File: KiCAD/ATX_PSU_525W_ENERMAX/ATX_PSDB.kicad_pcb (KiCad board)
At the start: 2 copper layers, 160 x 170 mm, 92 parts, among them J1 Fan1, J10 ATX12V1 8 Pin, J11 Current Sens, J12 Molex: 0039281243, J13 12V2, J14 Molex: 0039281243, J15 Potti, J16 Potti, J17 LED Yellow, J18 LED Yellow, J19 Volt Sens, J2 Power On Switch, J20 12V Out, J21 Volt Sens, J22 12V Out, J23 Molex: 0039281243, J24 Current Sens, J25 Current Sens, J26 Molex: 0039281243, J27 Molex: 0039281243, J28 Fan1, J29 Fan1, J3 Standby LED, J30 Potti, J31 Potti, J32 LED Red, J33 LED Orange, J34 Volt Sens, J35 5V Out, J36 Volt Sens, J37 3.3V Out, J38 Screw_Terminal_01x06, J39 Screw_Terminal_01x06, J4 ATX12V1, J40 Current Sens, J41 Current Sens, J42 Screw_Terminal_01x06, J43 Screw_Terminal_01x06, J44 Screw_Terminal_01x12, J5 Potti, J6 LED Yellow, J7 Volt Sens, J8 12V Out, J9 Main ATX 24Pin, Q1 Q_NMOS_DGS, Q2 Q_NMOS_DGS, Q3 Q_NMOS_DGS, Q4 Q_NMOS_DGS, Q5 Q_NMOS_DGS, U1 ACS712xLCTR-20A, U2 ACS712xLCTR-20A, U3 ACS712xLCTR-20A, U4 ACS712xLCTR-20A, U5 ACS712xLCTR-20A

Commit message: cleanup
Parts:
- removed HS1: Heatsink, Heatsink:Heatsink_Stonecold_HS-132_32x14mm_2xFixation1.5mm
- DZ1, DZ2, DZ3, DZ4, DZ5: value D_Zener_ALT -> TSV Protection Diode
- J10: value ATX12V1 8 Pin -> ATX12V1
- J12, J14: value Molex: 0039281243 -> Molex: 12V2
- J23, J26, J27: value Molex: 0039281243 -> Molex: 12V3
- J38: value Screw_Terminal_01x06 -> Terminal: 12V2; footprint TerminalBlock_WAGO:TerminalBlock_WAGO_236-108_1x08_P5.00mm_45Degree -> TerminalBlock_WAGO:TerminalBlock_WAGO_236-106_1x06_P5.00mm_45Degree
- J39: value Screw_Terminal_01x06 -> Terminal: 12V3; footprint TerminalBlock_WAGO:TerminalBlock_WAGO_236-108_1x08_P5.00mm_45Degree -> TerminalBlock_WAGO:TerminalBlock_WAGO_236-106_1x06_P5.00mm_45Degree
- J42: value Screw_Terminal_01x06 -> 5V Terminal; footprint TerminalBlock_WAGO:TerminalBlock_WAGO_236-108_1x08_P5.00mm_45Degree -> TerminalBlock_WAGO:TerminalBlock_WAGO_236-106_1x06_P5.00mm_45Degree
- J43: value Screw_Terminal_01x06 -> 3.3V Terminal; footprint TerminalBlock_WAGO:TerminalBlock_WAGO_236-108_1x08_P5.00mm_45Degree -> TerminalBlock_WAGO:TerminalBlock_WAGO_236-106_1x06_P5.00mm_45Degree
- J44: value Screw_Terminal_01x12 -> Ground Terminal
- Q1, Q2, Q3, Q4, Q5: value Q_NMOS_DGS -> Power N-Mosfet
- REF** (x4): value MountingHole_4.3mm_M4_Pad_Via -> Mounting Hole
- U1, U2, U3, U4, U5: value ACS712xLCTR-20A -> ACS712-20A
- moved REF** 185.8 mm to (83.8, 199.1), turned to 90 degrees
- moved REF** 10.7 mm to (86.4, 214.0)
- moved J13 10.2 mm to (125.7, 152.9)
- moved J26 10.2 mm to (125.7, 185.9)
- moved J12 10.2 mm to (110.5, 152.9)
- moved J14 10.2 mm to (95.2, 152.9)
- moved J23 10.2 mm to (110.5, 185.9)
- moved J27 10.2 mm to (95.2, 185.9)
- moved J38 10.2 mm to (96.0, 169.7)
- moved J39 10.2 mm to (96.5, 203.7)
- moved REF** 8.82 mm to (84.3, 57.7)
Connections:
- REF** pad 1: (no net) -> GND (x4)
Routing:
- net +5V: track 345.8 -> 598.8 mm, vias 0 -> 5
- net +3.3V: track 57.5 -> 45.7 mm
- net Net-(J7-Pad1): vias 0 -> 3
- net Net-(J36-Pad1): vias 0 -> 3
- net Net-(J34-Pad1): vias 0 -> 3
- net Net-(J21-Pad1): vias 0 -> 3
- net Net-(J19-Pad1): vias 0 -> 3
- net Net-(DZ5-Pad1): vias 0 -> 3
- net Net-(DZ4-Pad1): vias 0 -> 3
- net Net-(DZ3-Pad1): vias 0 -> 3
- net Net-(DZ2-Pad1): vias 0 -> 3
- net Net-(DZ1-Pad1): vias 0 -> 3
- net GND: vias 0 -> 67
- net (no net): vias 0 -> 2
- added copper zone on B.Cu, net +12V1
- added copper zone on B.Cu, net +12V2
- added copper zone on B.Cu, net +12V3
- added copper zone on B.Cu, net +3.3V
- added copper zone on B.Cu, net +5V
- added copper zone on B.Cu, net 12V1-
- added copper zone on B.Cu, net 12V2-
- added copper zone on B.Cu, net 12V3-
- added copper zone on B.Cu, net 3.3V-
- added copper zone on B.Cu, net 5V-
- added copper zone on B.Cu, net Net-(DZ1-Pad1)
- added copper zone on B.Cu, net Net-(DZ2-Pad1)
- added copper zone on B.Cu, net Net-(DZ3-Pad1)
- added copper zone on B.Cu, net Net-(DZ4-Pad1)
- added copper zone on B.Cu, net Net-(DZ5-Pad1)
- added copper zone on B.Cu, net Net-(J19-Pad1)
- added copper zone on B.Cu, net Net-(J21-Pad1)
- added copper zone on B.Cu, net Net-(J34-Pad1)
- added copper zone on B.Cu, net Net-(J36-Pad1)
- added copper zone on B.Cu, net Net-(J7-Pad1)

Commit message: labeling
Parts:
- removed the REF** at (224.0, 213.9)
- removed the REF** at (86.4, 214.0)
- added REF**: Mounting Hole, MountingHole:MountingHole_4.3mm_M4_Pad_Via, F.Cu at (223.9, 213.9)
- added REF**: Mounting Hole, MountingHole:MountingHole_4.3mm_M4_Pad_Via, F.Cu at (76.6, 214.0)
- J1: value Fan1 -> Fan 12V
- J2: value Power On Switch -> Power On/Off Switch
- J20: value 12V Out -> 12V2 Out
- J22: value 12V Out -> 12V3 Out
- J28: value Fan1 -> Fan 5V
- J29: value Fan1 -> Fan 3.3V
- J8: value 12V Out -> 12V1 Out
- moved REF** 131.1 mm to (80.4, 68.1)
- moved REF** 8.08 mm to (76.6, 55.4)
- moved REF** 2.07 mm to (223.9, 55.4)
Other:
- board text added: "12V1 Power Rail Input"
- board text added: "12V2 Power Rail Input"
- board text added: "3.3V Input Terminal"
- board text added: "5V Input Terminal"
- board text added: "Fuse Ratings should not exceed 10A each"
- board text added: "Molex"
- board text added: "Power Shunt"
- board text added: "Terminal"
- board text added: "Use Pottis for current limiting"

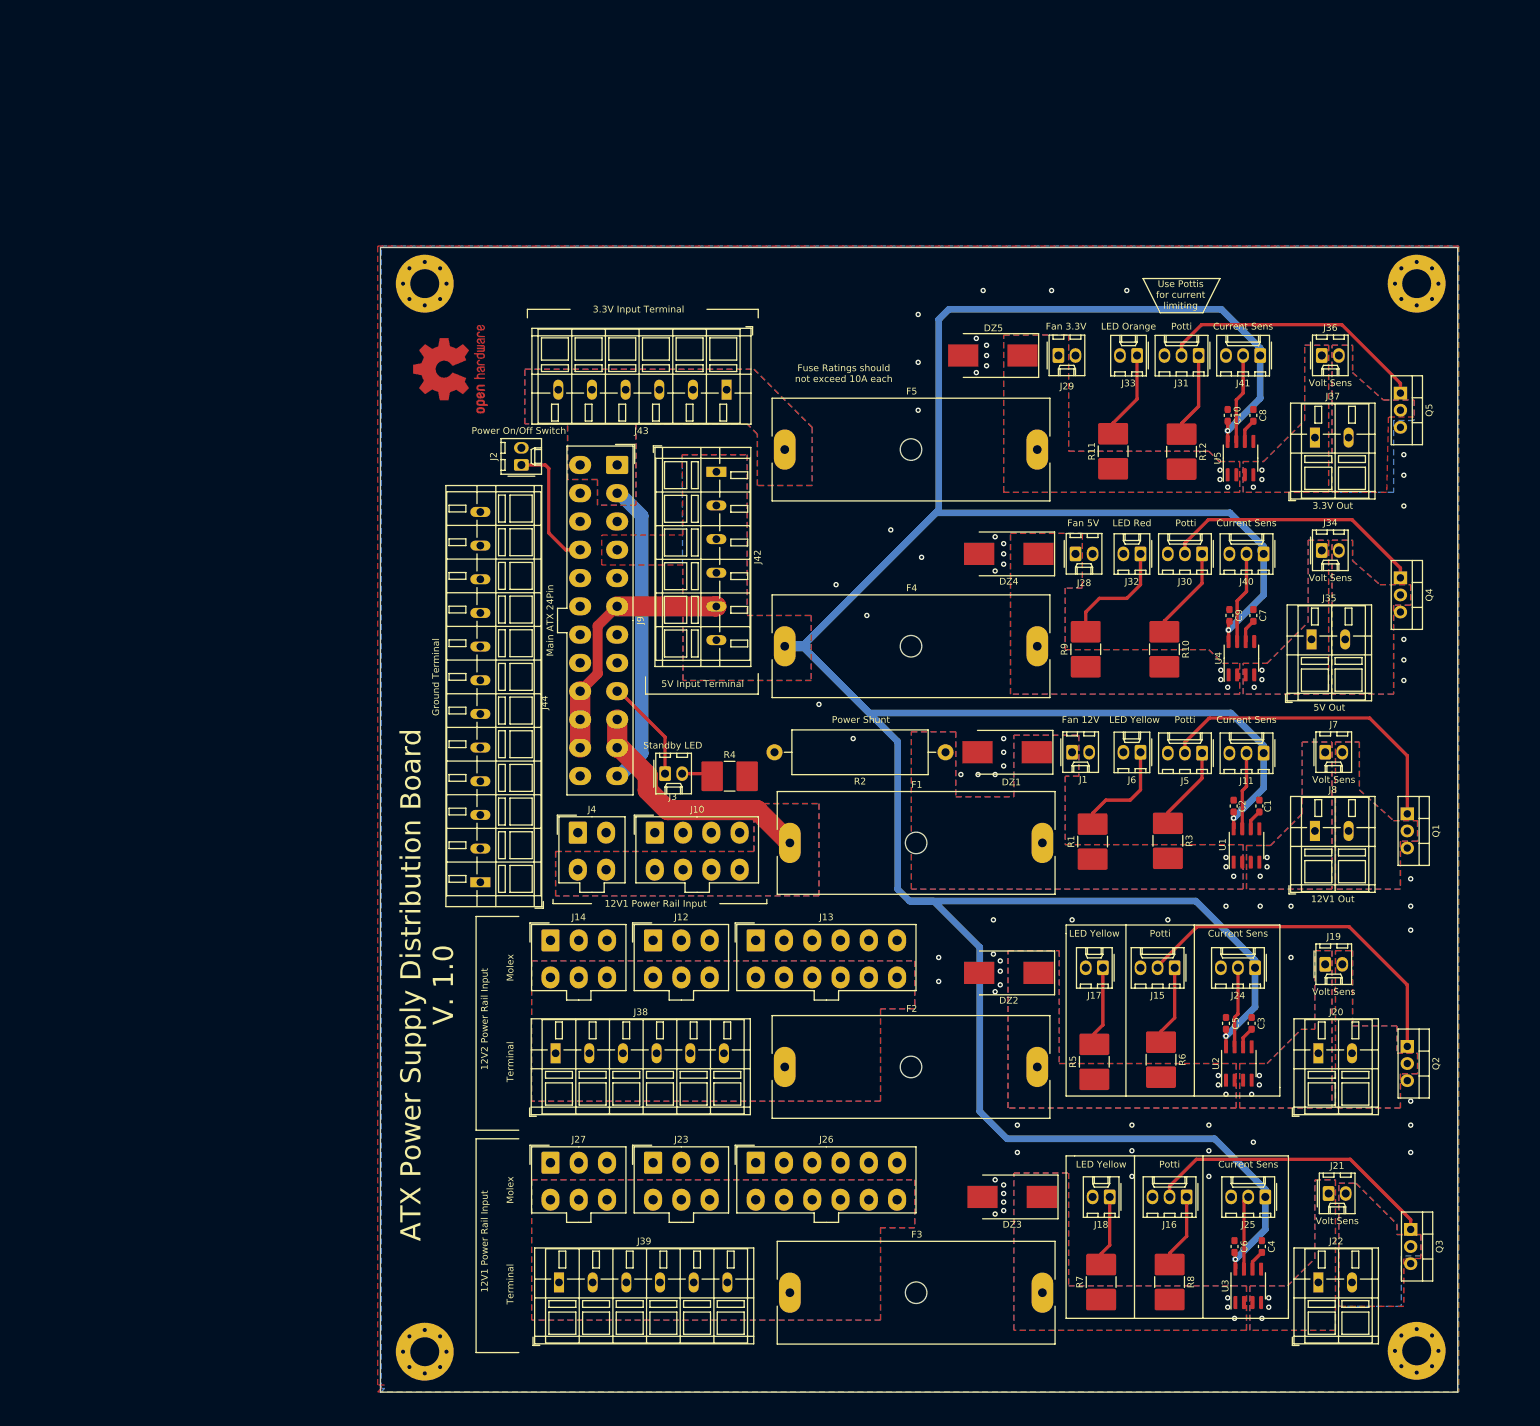
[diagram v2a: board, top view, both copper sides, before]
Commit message: refit traces, added global label added text
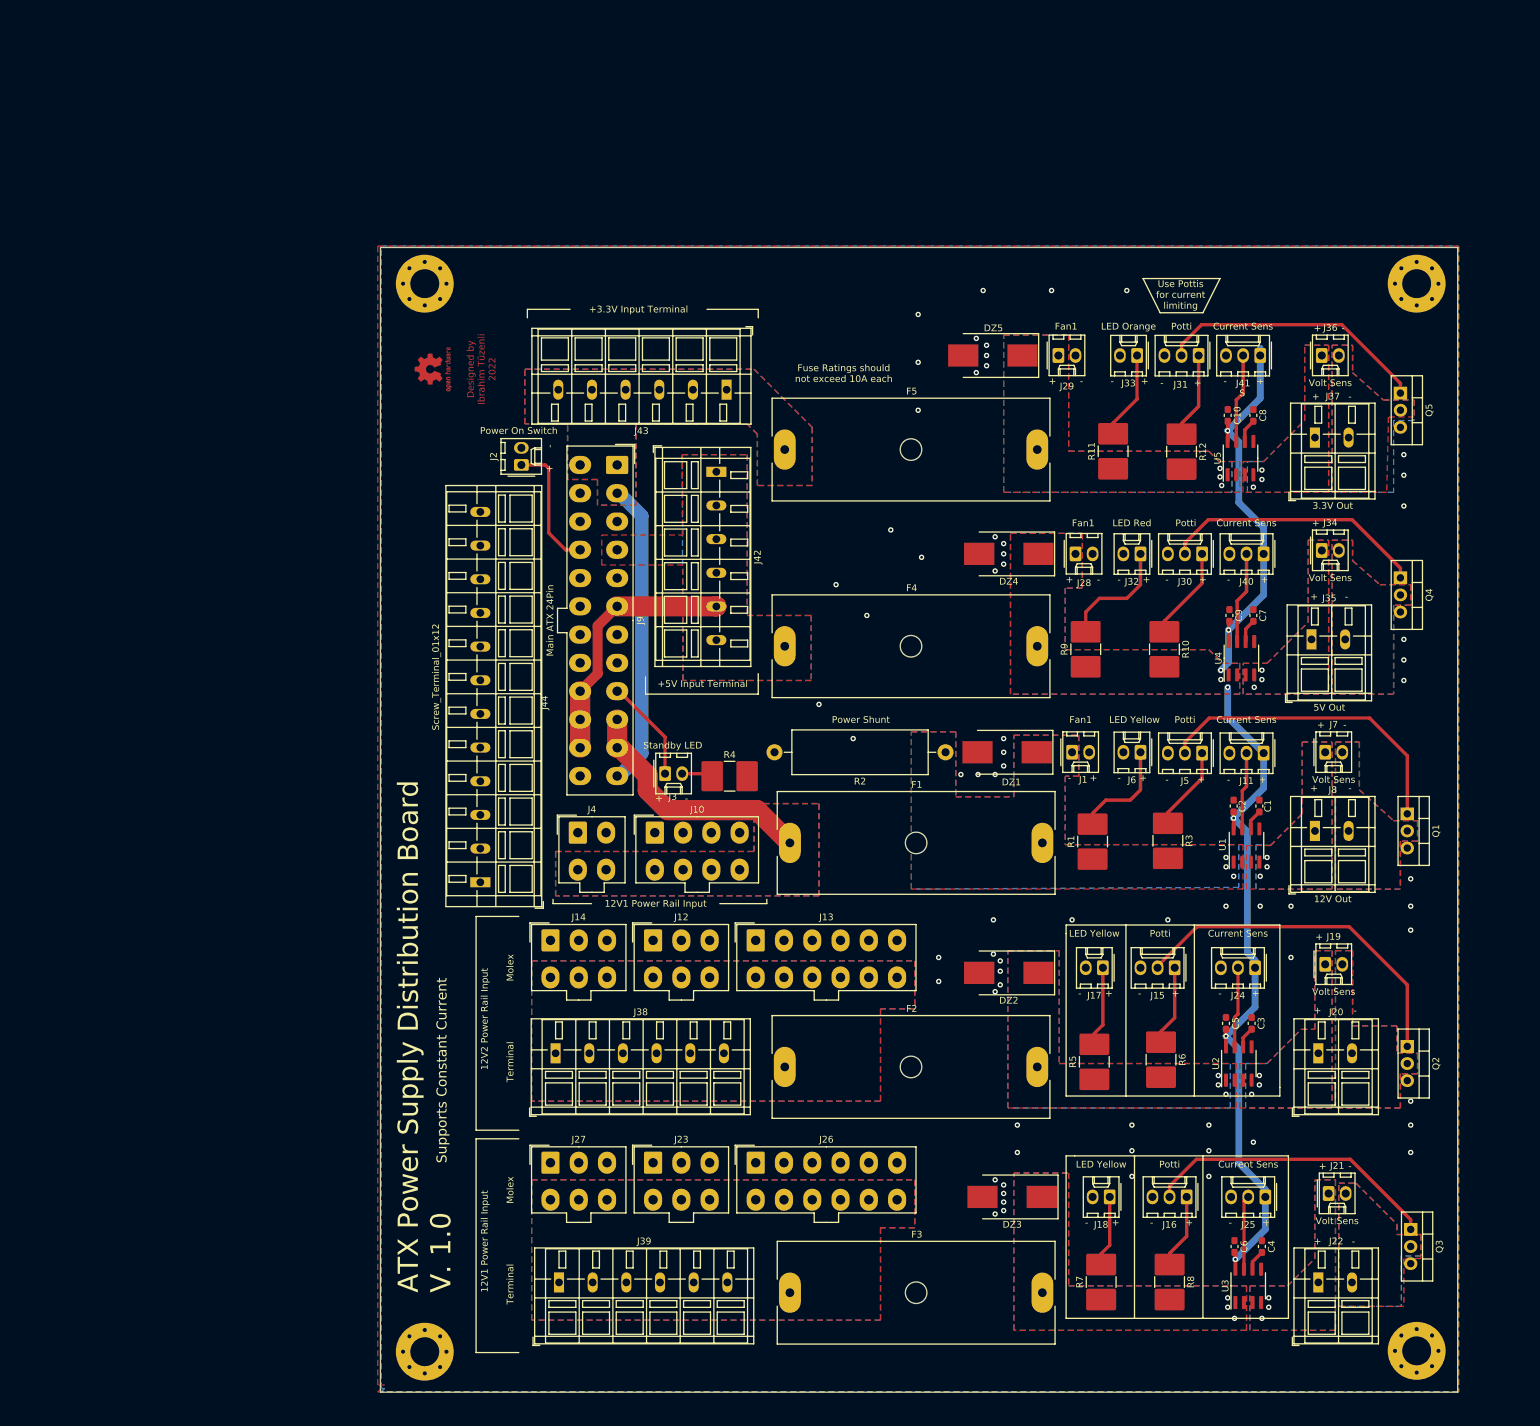
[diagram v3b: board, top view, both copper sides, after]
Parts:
- removed the REF** at (80.4, 68.1)
- added REF**: OSHW, Symbol:OSHW-Logo2_7.3x6mm_Copper, F.Cu at (77.9, 68.1)
- DZ1, DZ2, DZ3, DZ4, DZ5: value TSV Protection Diode -> D_Zener_ALT
- J1: value Fan 12V -> Fan1
- J10: value ATX12V1 -> ATX12V1 8 Pin
- J12, J14: value Molex: 12V2 -> Molex: 0039281243
- J2: value Power On/Off Switch -> Power On Switch
- J20: value 12V2 Out -> 12V Out
- J22: value 12V3 Out -> 12V Out
- J23, J26, J27: value Molex: 12V3 -> Molex: 0039281243
- J28: value Fan 5V -> Fan1
- J29: value Fan 3.3V -> Fan1
- J38: value Terminal: 12V2 -> Screw_Terminal_01x06
- J39: value Terminal: 12V3 -> Screw_Terminal_01x06
- J42: value 5V Terminal -> Screw_Terminal_01x06
- J43: value 3.3V Terminal -> Screw_Terminal_01x06
- J44: value Ground Terminal -> Screw_Terminal_01x12
- J8: value 12V1 Out -> 12V Out
- Q1, Q2, Q3, Q4, Q5: value Power N-Mosfet -> Q_NMOS_DGS
- U1, U2, U3, U4, U5: value ACS712-20A -> ACS712xLCTR-20A
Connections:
- DZ4 pad 1: Net-(DZ4-Pad1) -> +5V
- F4 pad 2: Net-(DZ4-Pad1) -> +5V
- J28 pad 1: Net-(DZ4-Pad1) -> +5V
- R10 pad 2: Net-(DZ4-Pad1) -> +5V
- R9 pad 1: Net-(DZ4-Pad1) -> +5V
- U4 pad 1: Net-(DZ4-Pad1) -> +5V
- U4 pad 2: Net-(DZ4-Pad1) -> +5V
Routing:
- net +5V: track 598.8 -> 204.2 mm, vias 5 -> 8
- net Net-(DZ4-Pad1): vias 3 -> 0
- removed copper zone on B.Cu, net Net-(DZ4-Pad1)
- removed copper zone on F.Cu, net Net-(DZ4-Pad1)
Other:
- board text added: "+"
- board text added: "+3.3V Input Terminal"
- board text added: "+5V Input Terminal"
- board text added: "-"
- board text added: "Designed by Ibrahim Tüzenli 2022"
- board text added: "S"
- board text added: "Supports Constant Current"
- board text removed: "3.3V Input Terminal"
- board text removed: "5V Input Terminal"

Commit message: Corrections and so on
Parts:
- J20: value 12V Out -> 12V2 Out
- J22: value 12V Out -> 12V3 Out
- J23: value Molex: 0039281243 -> Molex: 12V3 Input
- J39: value Screw_Terminal_01x06 -> Terminal: 12V3 Input
- J8: value 12V Out -> 12V1 Out
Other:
- board text added: "D"
- board text added: "G"
- board text added: "Supports Constant Current (10A Max each power rail)"
- board text removed: "Supports Constant Current"
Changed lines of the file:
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@@
   (general
     (thickness 1.6)
-    (drawings 129)
+    (drawings 145)
     (tracks 259)
     (zones 0)
@@
       (drillshape 0)
       (scaleselection 1)
-      (outputdirectory ""))
+      (outputdirectory "gerber/"))
   )
   (net 0 "")
@@
       (effects (font (size 1 1) (thickness 0.15)))
     )
-    (fp_text value "12V Out" (at 2.65 10.12) (layer F.Fab)
+    (fp_text value "12V3 Out" (at 2.65 10.12) (layer F.SilkS)
       (effects (font (size 1 1) (thickness 0.15)))
     )
@@
       (effects (font (size 1 1) (thickness 0.15)))
     )
-    (fp_text value "Molex: 0039281243" (at 4.2 9.95) (layer F.Fab)
+    (fp_text value "Molex: 12V3 Input" (at 4.2 9.95) (layer F.Fab)
       (effects (font (size 1 1) (thickness 0.15)))
     )
@@
       (effects (font (size 1 1) (thickness 0.15)))
     )
-    (fp_text value "12V Out" (at 2.65 10.12) (layer F.SilkS)
+    (fp_text value "12V1 Out" (at 2.65 10.12) (layer F.SilkS)
       (effects (font (size 1 1) (thickness 0.15)))
     )
@@
       (effects (font (size 1 1) (thickness 0.15)))
     )
-    (fp_text value "12V Out" (at 2.65 10.12) (layer F.Fab)
+    (fp_text value "12V2 Out" (at 2.65 10.12) (layer F.SilkS)
       (effects (font (size 1 1) (thickness 0.15)))
     )
@@
       (effects (font (size 1 1) (thickness 0.15)))
     )
-    (fp_text value Screw_Terminal_01x06 (at 12.65 10.12) (layer F.Fab)
+    (fp_text value "Terminal: 12V3 Input" (at 12.65 10.12) (layer F.Fab)
       (effects (font (size 1 1) (thickness 0.15)))
     )
@@
     )
   )
+  (gr_text G (at 225.552 195.072) (layer F.SilkS)
+    (effects (font (size 1 1) (thickness 0.25)))
+  )
+  (gr_text S (at 225.552 201.676) (layer F.SilkS)
+    (effects (font (size 1 1) (thickness 0.25)))
+  )
+  (gr_text D (at 225.552 198.501) (layer F.SilkS)
+    (effects (font (size 1 1) (thickness 0.25)))
+  )
+  (gr_text G (at 225.044 168.021) (layer F.SilkS)
+    (effects (font (size 1 1) (thickness 0.25)))
+  )
+  (gr_text S (at 225.044 174.625) (layer F.SilkS)
+    (effects (font (size 1 1) (thickness 0.25)))
+  )
+  (gr_text D (at 225.044 171.45) (layer F.SilkS)
+    (effects (font (size 1 1) (thickness 0.25)))
+  )
+  (gr_text G (at 225.044 133.35) (layer F.SilkS)
+    (effects (font (size 1 1) (thickness 0.25)))
+  )
+  (gr_text S (at 225.044 139.954) (layer F.SilkS)
+    (effects (font (size 1 1) (thickness 0.25)))
+  )
+  (gr_text D (at 225.044 136.779) (layer F.SilkS)
+    (effects (font (size 1 1) (thickness 0.25)))
+  )
+  (gr_text G (at 224.028 98.298) (layer F.SilkS)
+    (effects (font (size 1 1) (thickness 0.25)))
+  )
+  (gr_text S (at 224.028 104.902) (layer F.SilkS)
+    (effects (font (size 1 1) (thickness 0.25)))
+  )
+  (gr_text D (at 224.028 101.727) (layer F.SilkS)
+    (effects (font (size 1 1) (thickness 0.25)))
+  )
+  (gr_text G (at 224.028 70.866) (layer F.SilkS)
+    (effects (font (size 1 1) (thickness 0.25)))
+  )
+  (gr_text S (at 224.028 77.47) (layer F.SilkS)
+    (effects (font (size 1 1) (thickness 0.25)))
+  )
+  (gr_text D (at 224.028 74.295) (layer F.SilkS)
+    (effects (font (size 1 1) (thickness 0.25)))
+  )
+  (gr_text - (at 213.741 152.4) (layer F.SilkS)
+    (effects (font (size 1 1) (thickness 0.15)))
+  )
   (gr_text + (at 111.379 131.826) (layer F.SilkS)
     (effects (font (size 1 1) (thickness 0.15)))
@@
     (effects (font (size 1 1) (thickness 0.125)))
   )
-  (gr_text "Supports Constant Current" (at 79.121 172.212 90) (layer F.SilkS)
-    (effects (font (size 1.5 1.5) (thickness 0.3)))
+  (gr_text "Supports Constant Current \n(10A Max each power rail)" (at 80.391 188.214 90) (layer F.SilkS)
+    (effects (font (size 1.5 1.5) (thickness 0.3)) (justify left))
   )
   (gr_text "\nDesigned by\nIbrahim Tüzenli\n2022\n" (at 84.201 68.072 90) (layer F.Cu)
@@
     (effects (font (size 1 1) (thickness 0.15)))
   )
-  (gr_text "Fuse Ratings should\nnot exceed 10A each" (at 138.811 68.707) (layer F.SilkS)
-    (effects (font (size 1 1) (thickness 0.15)))
+  (gr_text "Fuse Ratings should\nnot exceed 10A each" (at 129.921 68.834) (layer F.SilkS)
+    (effects (font (size 1 1) (thickness 0.15)) (justify left))
   )
   (gr_line (start 194.691 54.61) (end 183.261 54.61) (layer F.SilkS) (width 0.15))

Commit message: finalization Rev. 1.0
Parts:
- J10: value ATX12V1 8 Pin -> ATX 12V1 Input
- J12, J14: value Molex: 0039281243 -> Molex: ATX 12V2 Input
- J13: value 12V2 -> Molex: ATX 12V2 Input
- J20: value 12V2 Out -> 12V Out
- J22: value 12V3 Out -> 12V Out
- J23: value Molex: 12V3 Input -> Molex: ATX 12V3 Input
- J26, J27: value Molex: 0039281243 -> Molex: ATX 12V3 Input
- J38: value Screw_Terminal_01x06 -> Terminal: +12V2 Input
- J39: value Terminal: 12V3 Input -> Terminal: +12V3 Input
- J4: value ATX12V1 -> ATX 12V1 Input
- J42: value Screw_Terminal_01x06 -> Terminal: +5V Input
- J43: value Screw_Terminal_01x06 -> Terminal: +3.3V Input
- J44: value Screw_Terminal_01x12 -> Terminal: Ground
- J8: value 12V1 Out -> 12V Out
- moved R2 0.52 mm to (153.4, 125.1)
- moved DZ1 0.51 mm to (163.6, 125.0)
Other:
- board text added: "!"
- board text added: "ATX Power Supply Distribution Board Rev. 1.0"
- board text added: "C2,C5,C6, 0.1uF C9,C10 C1,C3,C4 1nF C7,C8"
- board text added: "Capacitors"
- board text added: "GND"
- board text removed: "ATX Power Supply Distribution Board V. 1.0"

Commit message: Added Trademark, cleanup and so on
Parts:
- removed the REF** at (77.9, 68.1)
- removed the REF** at (223.9, 213.9)
- removed the REF** at (76.6, 214.0)
- added G***: IboschTonosch, CustomFootPrints:robot40x40, F.Cu at (27.1, 32.8)
- added REF**: Mounting Hole, MountingHole:MountingHole_4.3mm_M4_Pad_Via, F.Cu at (169.8, 179.3)
- added REF**: Mounting Hole, MountingHole:MountingHole_4.3mm_M4_Pad_Via, F.Cu at (22.5, 179.5)
- moved DZ3 64.2 mm to (109.7, 156.5)
- moved C10 64.2 mm to (141.7, 40.4)
- moved C2 64.2 mm to (142.6, 98.4)
- moved C5 64.2 mm to (141.5, 130.7)
- moved C7 64.2 mm to (145.5, 70.1)
- moved C8 64.2 mm to (145.5, 40.4)
- moved C9 64.2 mm to (142.0, 70.1)
- moved DZ2 64.2 mm to (109.2, 123.2)
- moved DZ4 64.2 mm to (109.2, 61.0)
- moved DZ5 64.2 mm to (106.9, 31.5)
- moved F1 64.2 mm to (76.7, 103.9)
- moved F2 64.2 mm to (75.9, 137.2)
- moved F3 64.2 mm to (76.7, 170.7)
- moved F4 64.2 mm to (75.9, 74.7)
- moved F5 64.2 mm to (75.9, 45.5)
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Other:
- board text added: "© 2022 Ibrahim Tüzenli"
- board text removed: "Designed by Ibrahim Tüzenli 2022"
